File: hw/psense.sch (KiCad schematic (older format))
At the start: 2 parts

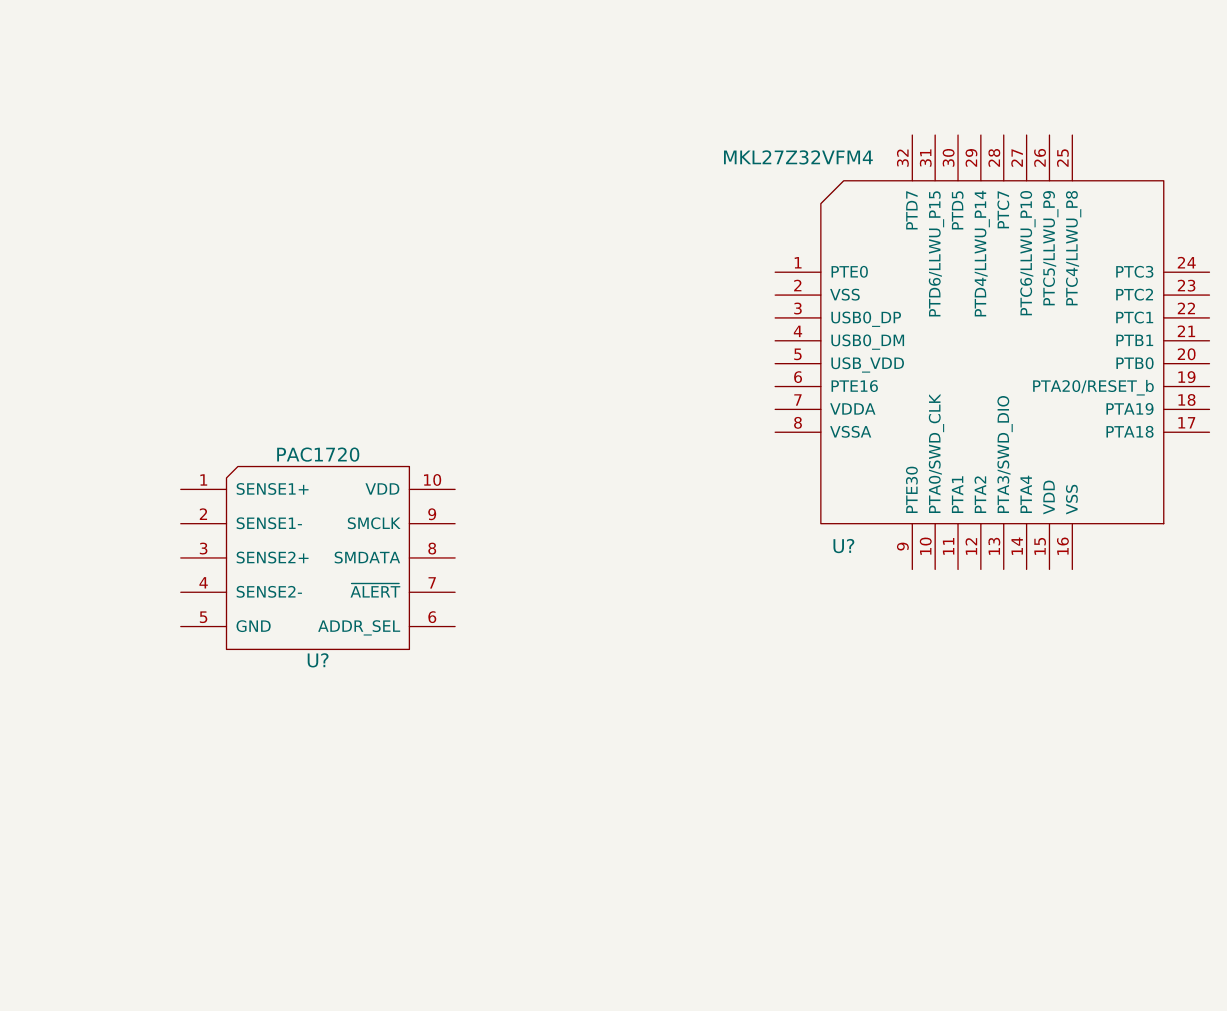
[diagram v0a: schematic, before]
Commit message: Swap mcu for plain old usb-i2c converter
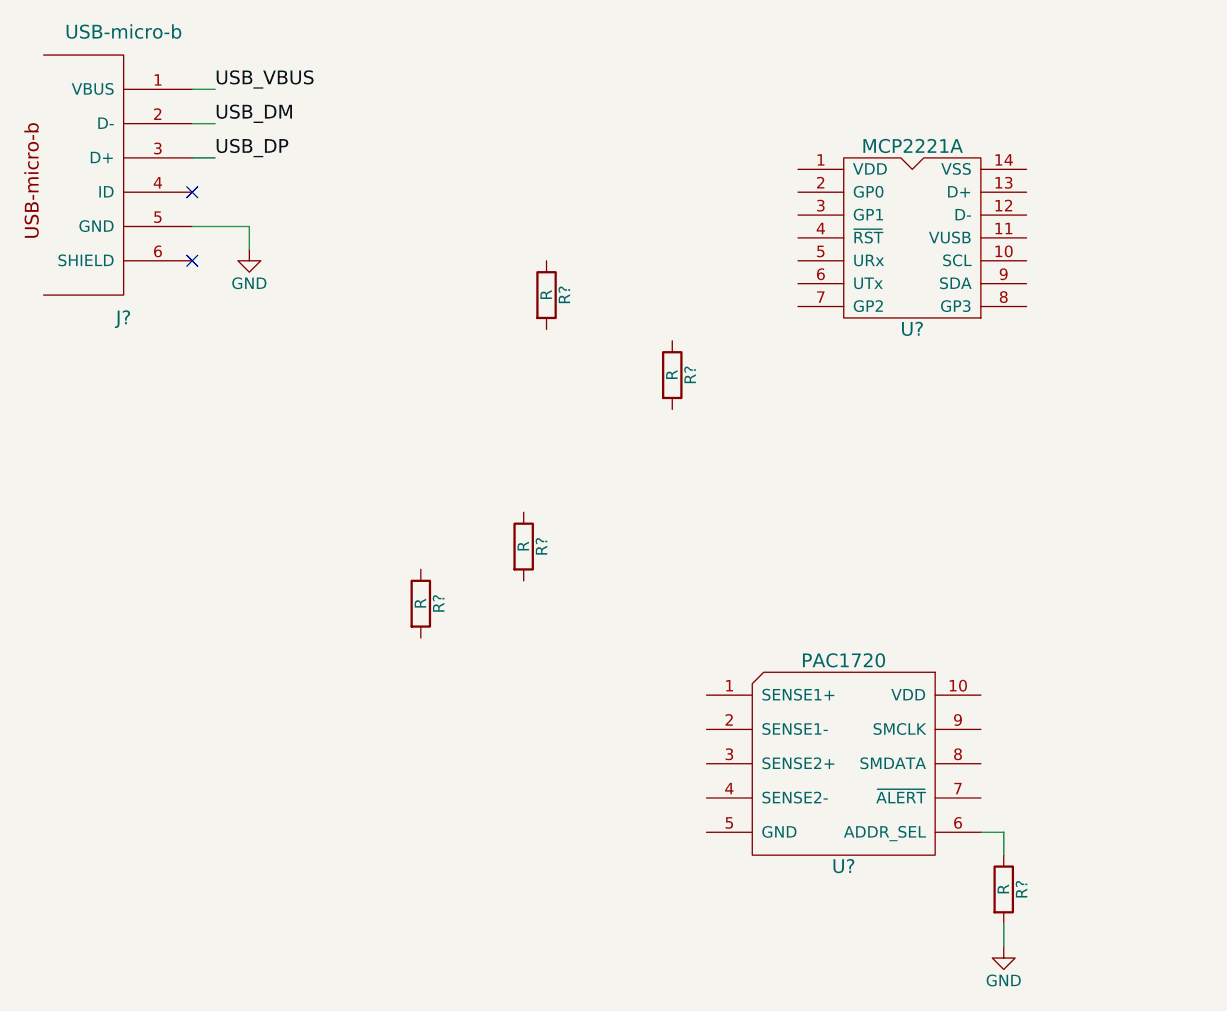
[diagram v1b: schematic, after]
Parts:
- removed U?: MKL27Z32VFM4, symbol MKL27Z32VFM4
- added J?: USB-micro-b, symbol USB-micro-b
- added R? (x5): R, symbol R
- added U?: MCP2221A, symbol MCP2221A
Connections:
- net at U?.6 (ADDR_SEL): now also R?.1
- new net GND: J?.5 (GND), R?.2
- new net USB_DM: J?.2 (D-)
- new net USB_DP: J?.3 (D+)
- new net USB_VBUS: J?.1 (VBUS)
- no-connect marks 0 -> 2
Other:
- moved on the sheet: U?
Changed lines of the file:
@@
 LIBS:valves
 LIBS:kicadlib
+LIBS:psense-cache
 EELAYER 25 0
 EELAYER END
@@
 L PAC1720 U?
 U 1 1 589BCEA6
-P 3000 4050
-F 0 "U?" H 3000 3600 60  0000 C CNN
-F 1 "PAC1720" H 3000 4500 60  0000 C CNN
-F 2 "" H 2800 4050 60  0001 C CNN
-F 3 "" H 2800 4050 60  0001 C CNN
-	1    3000 4050
+P 5300 4950
+F 0 "U?" H 5300 4500 60  0000 C CNN
+F 1 "PAC1720" H 5300 5400 60  0000 C CNN
+F 2 "" H 5100 4950 60  0001 C CNN
+F 3 "" H 5100 4950 60  0001 C CNN
+	1    5300 4950
 	1    0    0    -1
 $EndComp
 $Comp
-L MKL27Z32VFM4 U?
-U 1 1 589BD8C6
-P 5950 3200
-F 0 "U?" H 5300 2400 60  0000 C CNN
-F 1 "MKL27Z32VFM4" H 5100 4100 60  0000 C CNN
-F 2 "" H 5400 3350 60  0001 C CNN
-F 3 "" H 5400 3350 60  0001 C CNN
-	1    5950 3200
+L USB-micro-b J?
+U 1 1 58A07AEC
+P 2150 2400
+F 0 "J?" H 2150 1800 60  0000 C CNN
+F 1 "USB-micro-b" H 2150 3050 60  0000 C CNN
+F 2 "" H 2150 2400 60  0000 C CNN
+F 3 "" H 2150 2400 60  0000 C CNN
+	1    2150 2400
 	1    0    0    -1
 $EndComp
+$Comp
+L R R?
+U 1 1 58A07CAC
+P 4000 2900
+F 0 "R?" V 4080 2900 50  0000 C CNN
+F 1 "R" V 4000 2900 50  0000 C CNN
+F 2 "" V 3930 2900 50  0000 C CNN
+F 3 "" H 4000 2900 50  0000 C CNN
+	1    4000 2900
+	1    0    0    -1
+$EndComp
+$Comp
+L R R?
+U 1 1 58A07D17
+P 4550 3250
+F 0 "R?" V 4630 3250 50  0000 C CNN
+F 1 "R" V 4550 3250 50  0000 C CNN
+F 2 "" V 4480 3250 50  0000 C CNN
+F 3 "" H 4550 3250 50  0000 C CNN
+	1    4550 3250
+	1    0    0    -1
+$EndComp
+$Comp
+L R R?
+U 1 1 58A07D36
+P 3450 4250
+F 0 "R?" V 3530 4250 50  0000 C CNN
+F 1 "R" V 3450 4250 50  0000 C CNN
+F 2 "" V 3380 4250 50  0000 C CNN
+F 3 "" H 3450 4250 50  0000 C CNN
+	1    3450 4250
+	1    0    0    -1
+$EndComp
+$Comp
+L R R?
+U 1 1 58A07D59
+P 3900 4000
+F 0 "R?" V 3980 4000 50  0000 C CNN
+F 1 "R" V 3900 4000 50  0000 C CNN
+F 2 "" V 3830 4000 50  0000 C CNN
+F 3 "" H 3900 4000 50  0000 C CNN
+	1    3900 4000
+	1    0    0    -1
+$EndComp
+$Comp
+L R R?
+U 1 1 58A07E7D
+P 6000 5500
+F 0 "R?" V 6080 5500 50  0000 C CNN
+F 1 "R" V 6000 5500 50  0000 C CNN
+F 2 "" V 5930 5500 50  0000 C CNN
+F 3 "" H 6000 5500 50  0000 C CNN
+	1    6000 5500
+	1    0    0    -1
+$EndComp
+$Comp
+L GND #PWR?
+U 1 1 58A07EFF
+P 6000 5750
+F 0 "#PWR?" H 6000 5500 50  0001 C CNN
+F 1 "GND" H 6000 5600 50  0000 C CNN
+F 2 "" H 6000 5750 50  0000 C CNN
+F 3 "" H 6000 5750 50  0000 C CNN
+	1    6000 5750
+	1    0    0    -1
+$EndComp
+$Comp
+L GND #PWR?
+U 1 1 58A0804C
+P 2700 2700
+F 0 "#PWR?" H 2700 2450 50  0001 C CNN
+F 1 "GND" H 2700 2550 50  0000 C CNN
+F 2 "" H 2700 2700 50  0000 C CNN
+F 3 "" H 2700 2700 50  0000 C CNN
+	1    2700 2700
+	1    0    0    -1
+$EndComp
+NoConn ~ 2450 2750
+Text Label 2550 2000 0    60   ~ 0
+USB_VBUS
+Text Label 2550 2150 0    60   ~ 0
+USB_DM
+Text Label 2550 2300 0    60   ~ 0
+USB_DP
+NoConn ~ 2450 2450
+Wire Wire Line
+	6000 5750 6000 5650
+Wire Wire Line
+	6000 5350 6000 5250
+Wire Wire Line
+	6000 5250 5900 5250
+Wire Wire Line
+	2450 2600 2700 2600
+Wire Wire Line
+	2700 2600 2700 2700
+Wire Wire Line
+	2550 2300 2450 2300
+Wire Wire Line
+	2450 2150 2550 2150
+Wire Wire Line
+	2550 2000 2450 2000
+$Comp
+L MCP2221A U?
+U 1 1 58A08AC7
+P 5600 2650
+F 0 "U?" H 5600 2250 60  0000 C CNN
+F 1 "MCP2221A" H 5600 3050 60  0000 C CNN
+F 2 "" H 5600 2550 60  0001 C CNN
+F 3 "" H 5600 2550 60  0001 C CNN
+	1    5600 2650
+	1    0    0    -1
+$EndComp
